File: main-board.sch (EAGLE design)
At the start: 54 parts, among them IC1 MEGA328-PB, IC2 MCP73831, IC3 LE33, Q1 3,6864 MHz, Q4 TSM2302CX, T1 IRF7306

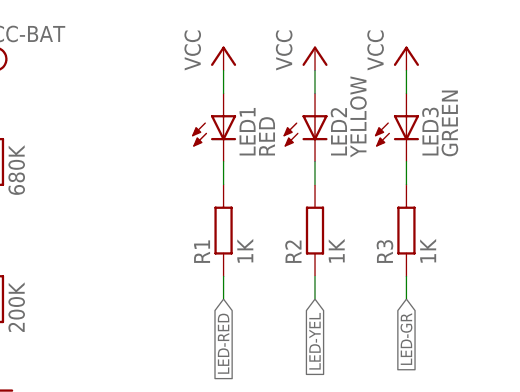
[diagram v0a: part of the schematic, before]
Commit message: Create nice place views.
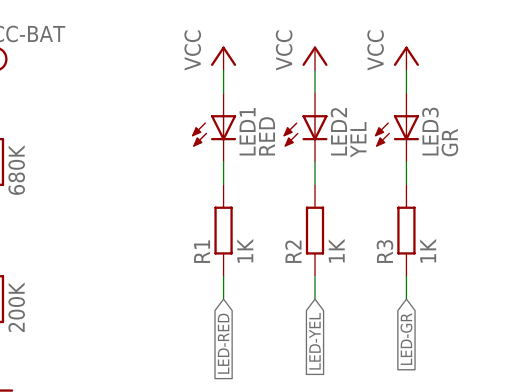
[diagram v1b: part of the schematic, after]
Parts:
- LED2: value YELLOW -> YEL
- LED3: value GREEN -> GR
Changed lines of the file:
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@@
 <part name="GND2" library="supply1" deviceset="GND" device=""/>
 <part name="LED1" library="led" deviceset="LED" device="CHIP-LED0805" value="RED"/>
-<part name="LED2" library="led" deviceset="LED" device="CHIP-LED0805" value="YELLOW"/>
-<part name="LED3" library="led" deviceset="LED" device="CHIP-LED0805" value="GREEN"/>
+<part name="LED2" library="led" deviceset="LED" device="CHIP-LED0805" value="YEL"/>
+<part name="LED3" library="led" deviceset="LED" device="CHIP-LED0805" value="GR"/>
 <part name="P+2" library="supply1" deviceset="VCC" device=""/>
 <part name="P+3" library="supply1" deviceset="VCC" device=""/>

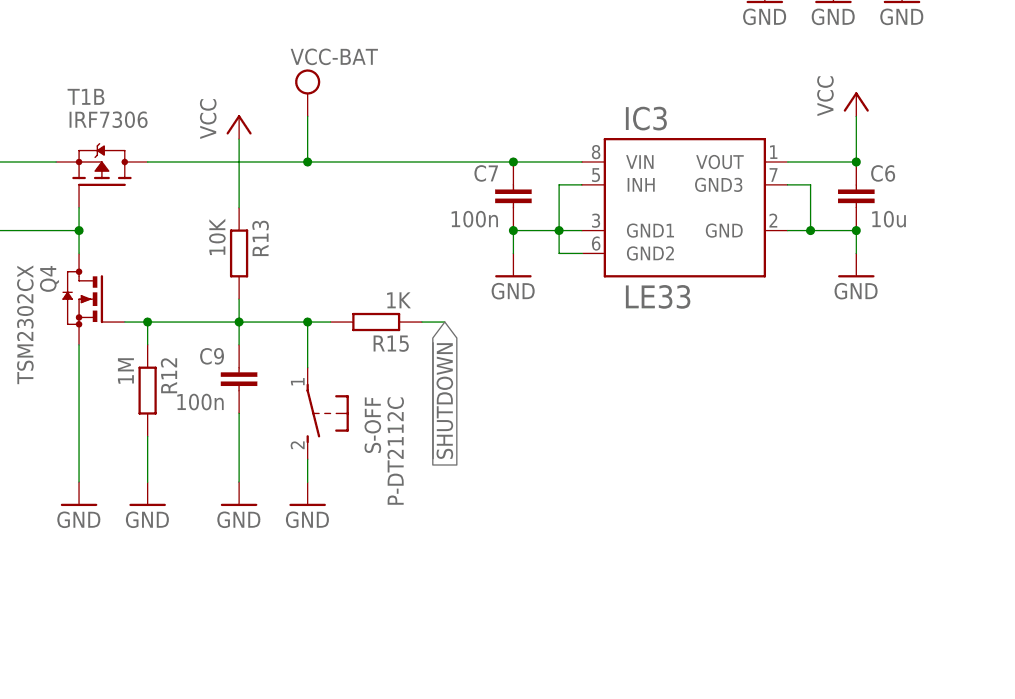
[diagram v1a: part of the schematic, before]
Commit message: Fix shutdown circuit.
Shutting down from CPU should work now.
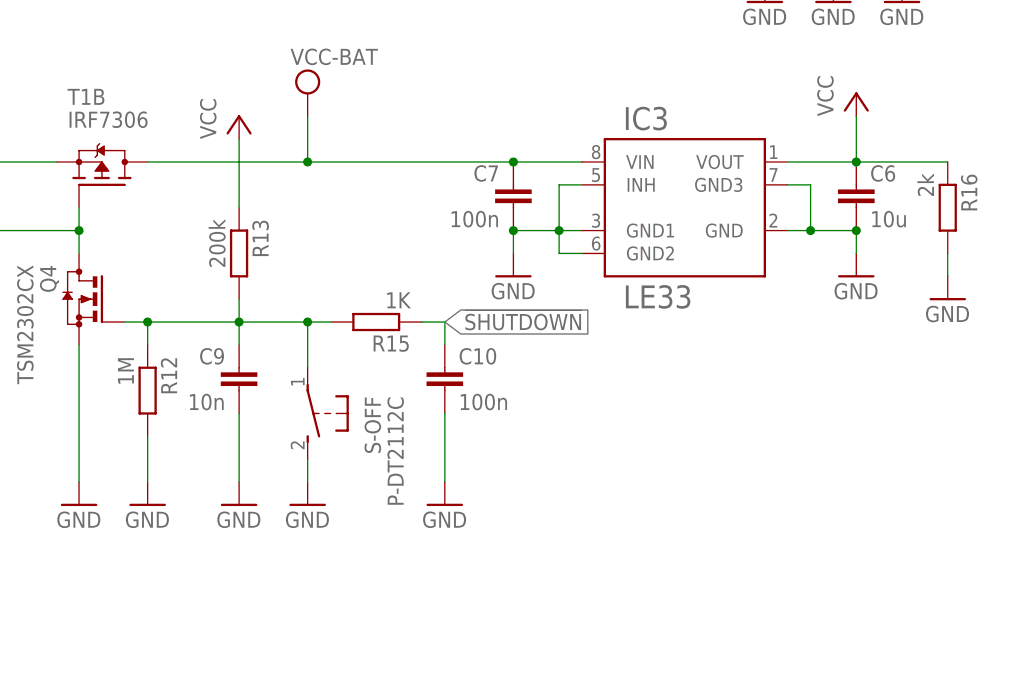
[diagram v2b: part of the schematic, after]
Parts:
- added C10: 100n, rcl:C-EUC0805
- added R16: 2k, rcl:R-EU_R0805
- C9: value 100n -> 10n
- R13: value 10K -> 200k
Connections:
- net !SHUTDOWN: now also C10.1
- net GND: now also C10.2, R16.2
- net VCC: now also R16.1
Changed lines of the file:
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@@
 <attributes>
 <attribute name="AUTHOR" value="Jan Horacek"/>
-<attribute name="VERSION" value="1.2"/>
+<attribute name="VERSION" value="1.3"/>
 </attributes>
 <variantdefs>
@@
 <part name="C8" library="rcl" deviceset="C-EU" device="C0805" value="10u"/>
 <part name="R12" library="rcl" deviceset="R-EU_" device="R0805" value="1M"/>
-<part name="R13" library="rcl" deviceset="R-EU_" device="R0805" value="10K"/>
-<part name="C9" library="rcl" deviceset="C-EU" device="C0805" value="100n"/>
+<part name="R13" library="rcl" deviceset="R-EU_" device="R0805" value="200k"/>
+<part name="C9" library="rcl" deviceset="C-EU" device="C0805" value="10n"/>
 <part name="R10" library="rcl" deviceset="R-EU_" device="R0805" value="100K"/>
 <part name="Q4" library="transistor-small-signal" deviceset="BSS123" device="" value="TSM2302CX"/>
@@
 <variant name="BASIC" populate="no"/>
 </part>
+<part name="C10" library="rcl" deviceset="C-EU" device="C0805" value="100n"/>
+<part name="GND19" library="supply1" library_urn="urn:adsk.eagle:library:371" deviceset="GND" device=""/>
+<part name="R16" library="rcl" deviceset="R-EU_" device="R0805" value="2k"/>
+<part name="GND20" library="supply1" deviceset="GND" device=""/>
 </parts>
 <sheets>
@@
 <attribute name="VALUE" x="50.5714" y="48.26" size="1.778" layer="96" rot="R90"/>
 </instance>
+<instance part="C10" gate="G$1" x="193.04" y="48.26"/>
+<instance part="GND19" gate="1" x="193.04" y="33.02"/>
+<instance part="R16" gate="G$1" x="248.92" y="66.04" rot="R270"/>
+<instance part="GND20" gate="1" x="248.92" y="55.88"/>
 </instances>
 <busses>
@@
 <wire x1="111.76" y1="58.42" x2="111.76" y2="66.04" width="0.1524" layer="91"/>
 </segment>
+<segment>
+<pinref part="GND19" gate="1" pin="GND"/>
+<pinref part="C10" gate="G$1" pin="2"/>
+<wire x1="193.04" y1="35.56" x2="193.04" y2="43.18" width="0.1524" layer="91"/>
+</segment>
+<segment>
+<pinref part="GND20" gate="1" pin="GND"/>
+<pinref part="R16" gate="G$1" pin="2"/>
+<wire x1="248.92" y1="58.42" x2="248.92" y2="60.96" width="0.1524" layer="91"/>
+</segment>
 </net>
 <net name="VCC" class="2">
@@
 <pinref part="C6" gate="G$1" pin="1"/>
 <junction x="238.76" y="71.12"/>
+<pinref part="R16" gate="G$1" pin="1"/>
+<wire x1="238.76" y1="71.12" x2="248.92" y2="71.12" width="0.1524" layer="91"/>
 </segment>
 <segment>
@@
 <pinref part="R15" gate="G$1" pin="1"/>
 <wire x1="193.04" y1="53.34" x2="190.5" y2="53.34" width="0.1524" layer="91"/>
-<label x="193.04" y="53.34" size="1.778" layer="95" rot="R270" xref="yes"/>
-</segment>
-<segment>
+<label x="193.04" y="53.34" size="1.778" layer="95" xref="yes"/>
+<pinref part="C10" gate="G$1" pin="1"/>
+<wire x1="193.04" y1="50.8" x2="193.04" y2="53.34" width="0.1524" layer="91"/>
+</segment>
+<segment>

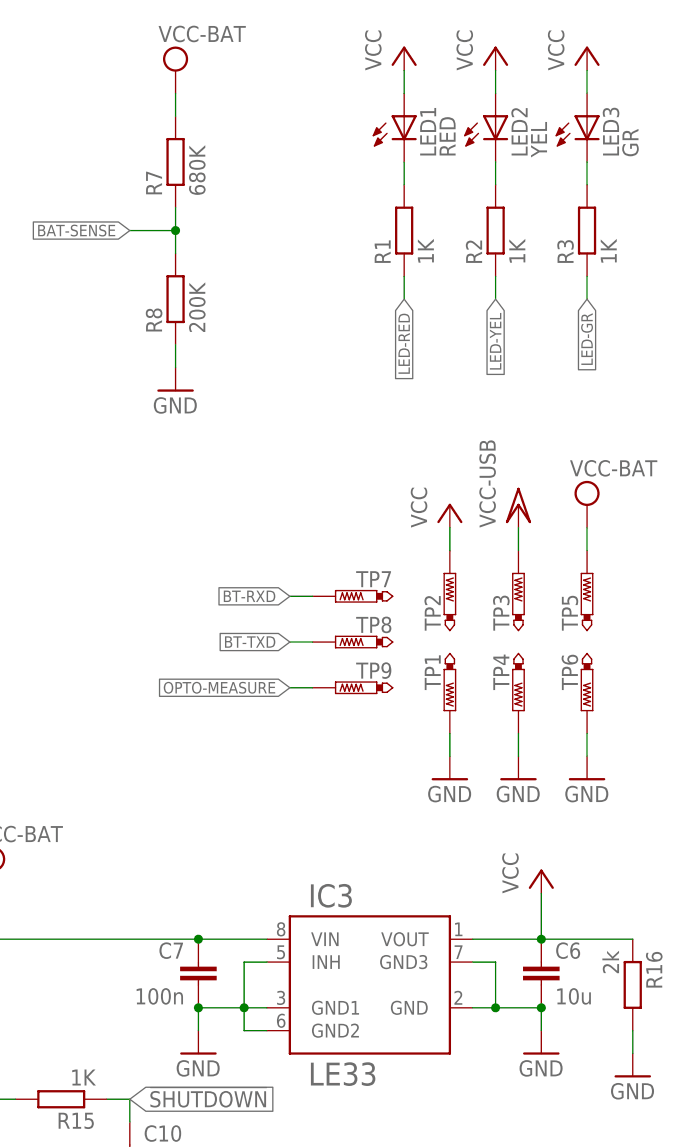
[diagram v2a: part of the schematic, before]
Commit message: Change voltage divisor (use LDO as reference).
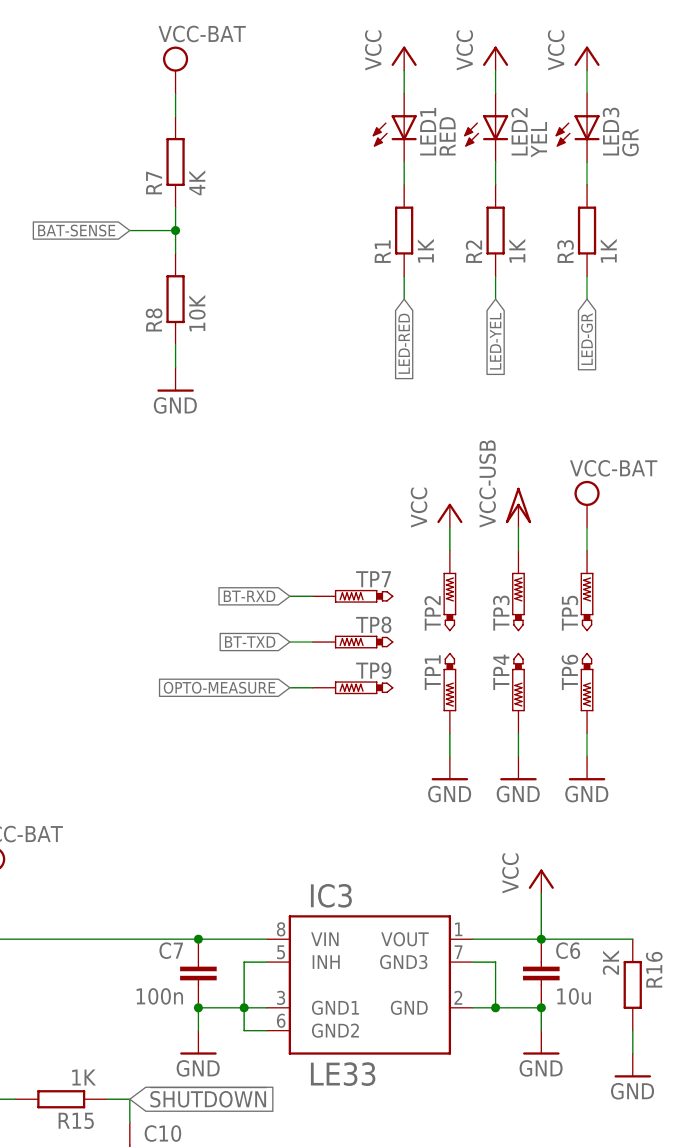
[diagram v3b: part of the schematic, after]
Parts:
- R16: value 2k -> 2K
- R7: value 680K -> 4K
- R8: value 200K -> 10K
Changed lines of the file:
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@@
 <part name="R6" library="rcl" deviceset="R-EU_" device="R0805" value="10K"/>
 <part name="P+8" library="supply1" deviceset="VCC" device=""/>
-<part name="R7" library="rcl" deviceset="R-EU_" device="R0805" value="680K"/>
-<part name="R8" library="rcl" deviceset="R-EU_" device="R0805" value="200K"/>
+<part name="R7" library="rcl" deviceset="R-EU_" device="R0805" value="4K"/>
+<part name="R8" library="rcl" deviceset="R-EU_" device="R0805" value="10K"/>
 <part name="SUPPLY1" library="supply2" deviceset="VCC" device="" value="VCC-BAT"/>
 <part name="GND7" library="supply1" deviceset="GND" device=""/>
@@
 <part name="C10" library="rcl" deviceset="C-EU" device="C0805" value="100n"/>
 <part name="GND19" library="supply1" library_urn="urn:adsk.eagle:library:371" deviceset="GND" device=""/>
-<part name="R16" library="rcl" deviceset="R-EU_" device="R0805" value="2k"/>
+<part name="R16" library="rcl" deviceset="R-EU_" device="R0805" value="2K"/>
 <part name="GND20" library="supply1" deviceset="GND" device=""/>
 </parts>

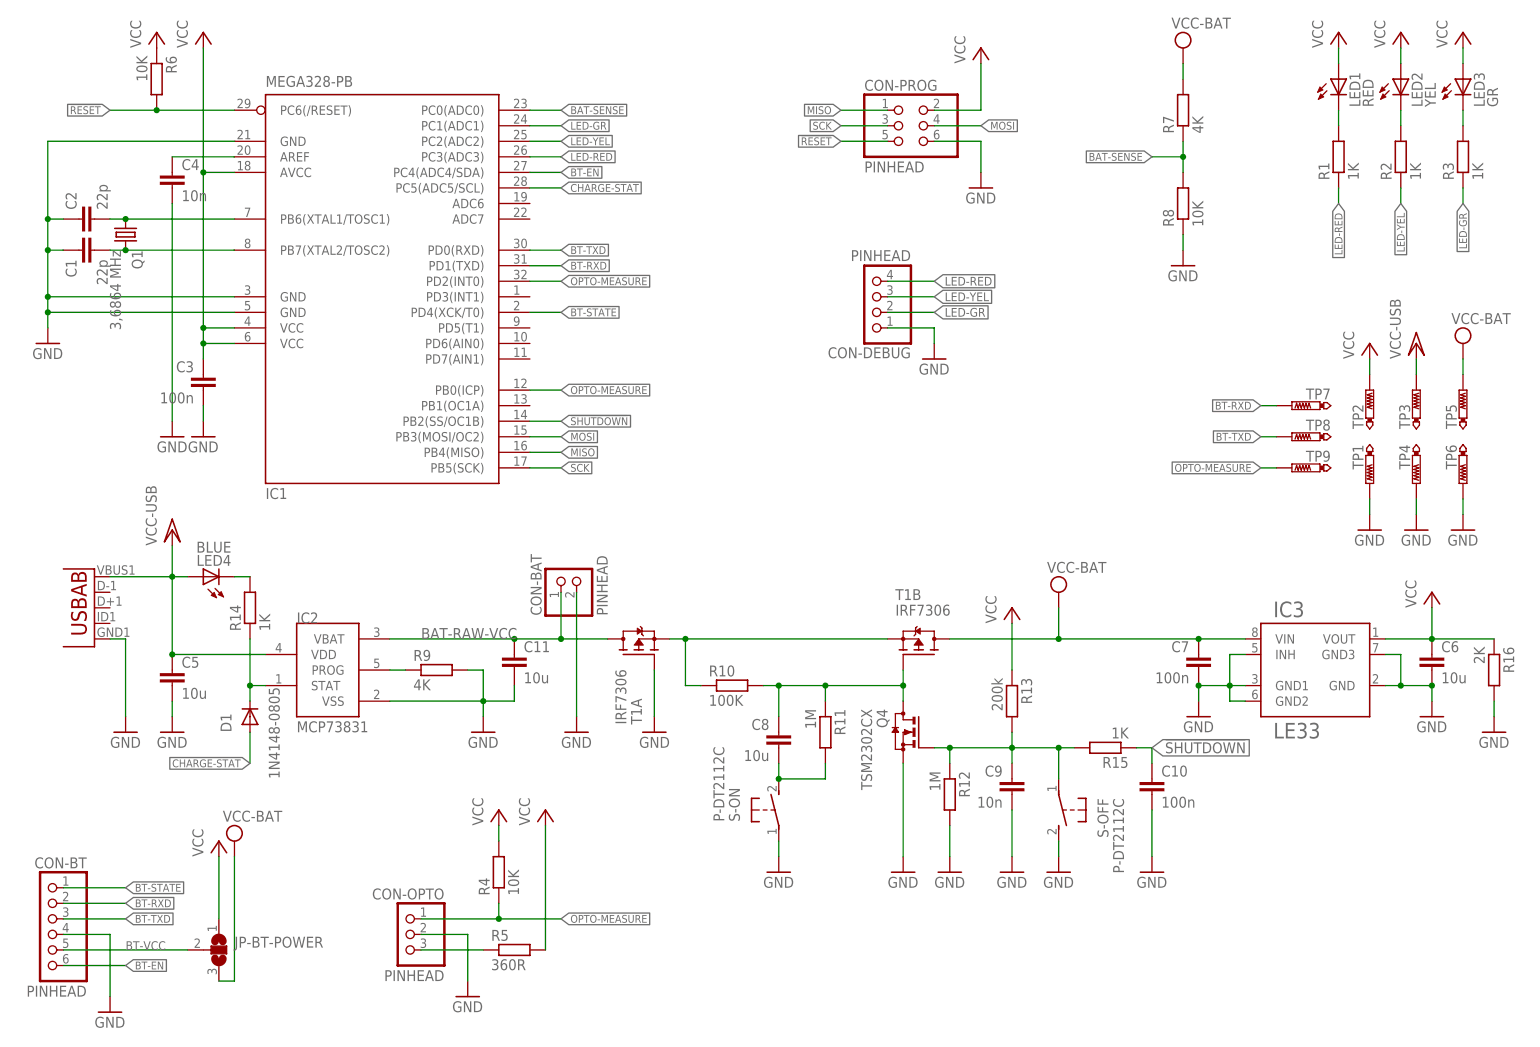
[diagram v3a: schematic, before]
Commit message: 4K -> 3K9.
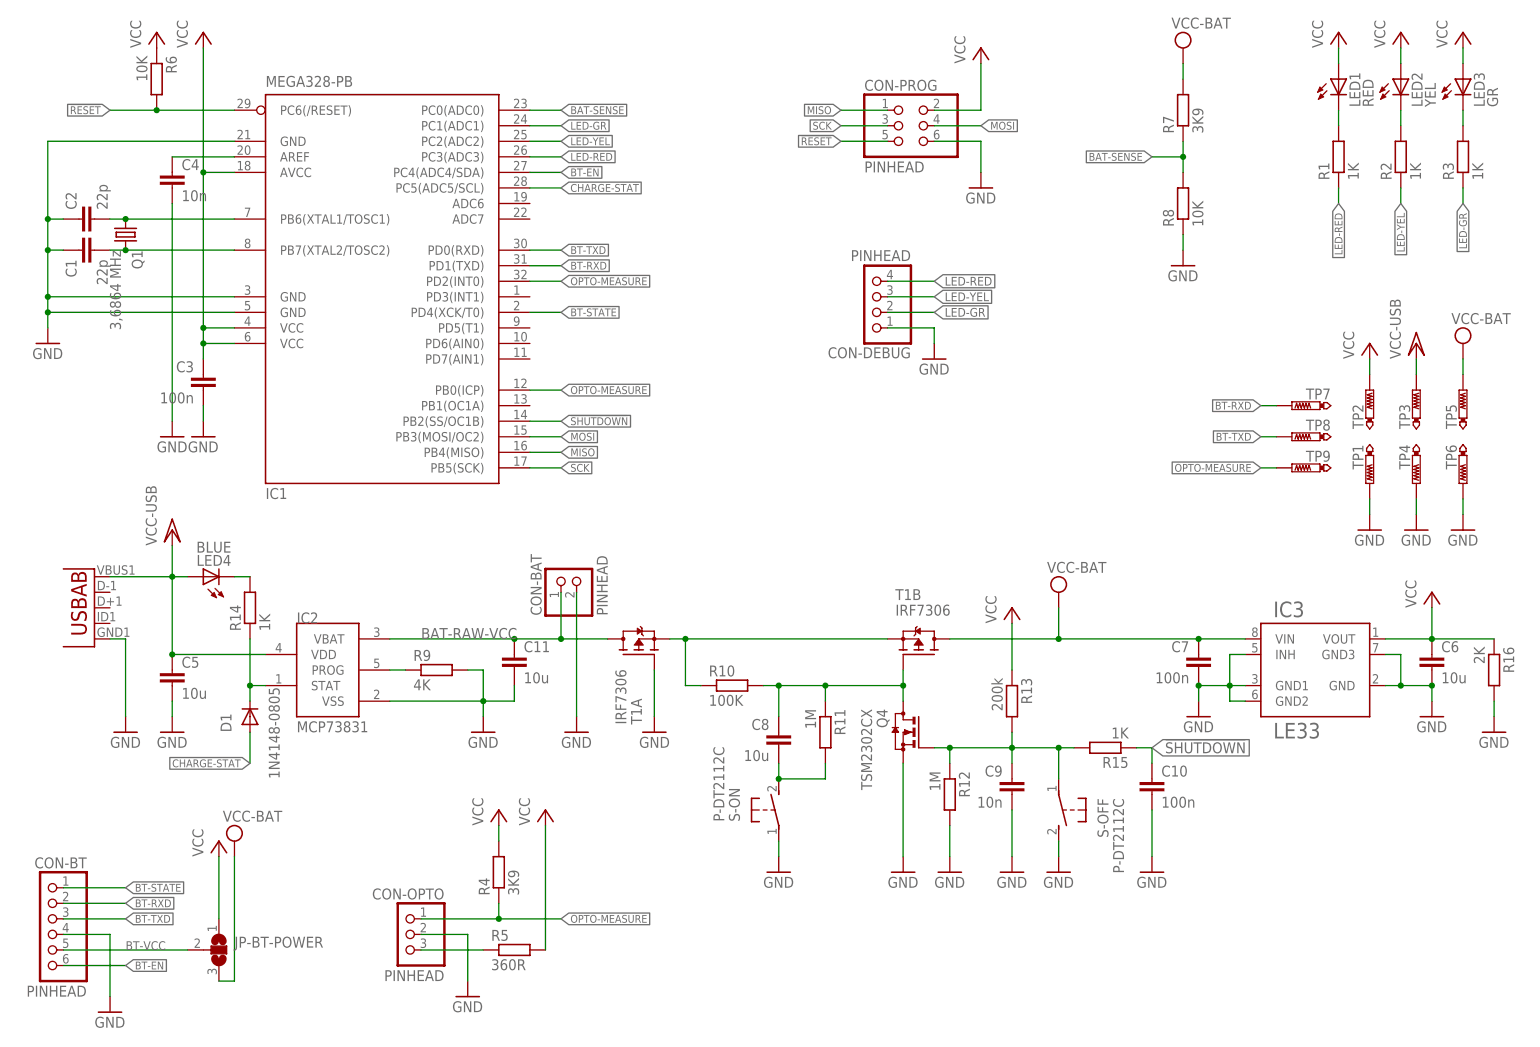
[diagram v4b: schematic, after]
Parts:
- R4: value 10K -> 3K9
- R7: value 4K -> 3K9
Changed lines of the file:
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@@
 <part name="CON-OPTO" library="pinhead" deviceset="PINHD-1X3" device="" value="PINHEAD"/>
 <part name="GND5" library="supply1" deviceset="GND" device=""/>
-<part name="R4" library="rcl" deviceset="R-EU_" device="R0805" value="10K"/>
+<part name="R4" library="rcl" deviceset="R-EU_" device="R0805" value="3K9"/>
 <part name="R5" library="rcl" deviceset="R-EU_" device="R0805" value="360R"/>
 <part name="P+6" library="supply1" deviceset="VCC" device=""/>
@@
 <part name="R6" library="rcl" deviceset="R-EU_" device="R0805" value="10K"/>
 <part name="P+8" library="supply1" deviceset="VCC" device=""/>
-<part name="R7" library="rcl" deviceset="R-EU_" device="R0805" value="4K"/>
+<part name="R7" library="rcl" deviceset="R-EU_" device="R0805" value="3K9"/>
 <part name="R8" library="rcl" deviceset="R-EU_" device="R0805" value="10K"/>
 <part name="SUPPLY1" library="supply2" deviceset="VCC" device="" value="VCC-BAT"/>

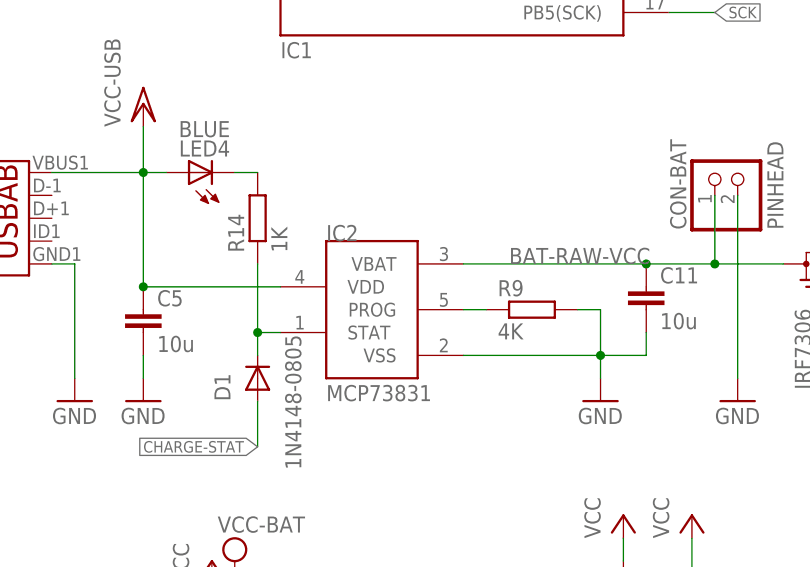
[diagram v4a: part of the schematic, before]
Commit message: Update values of resistors.
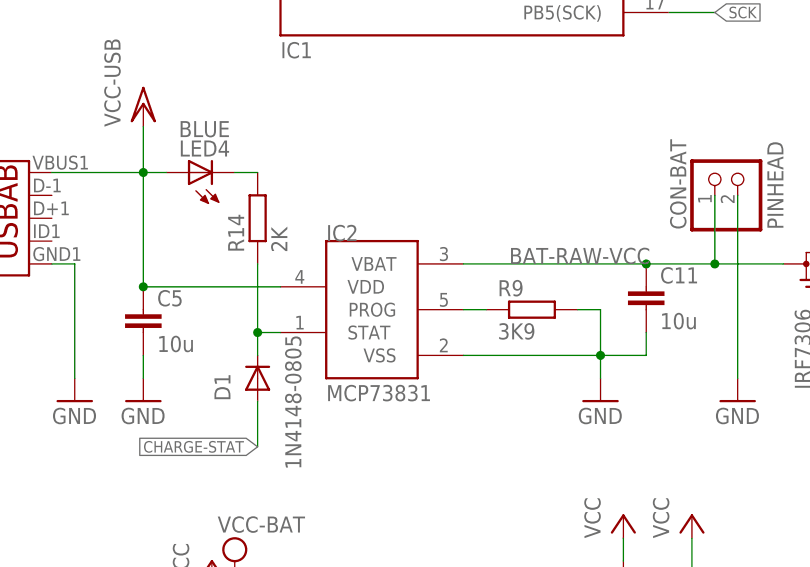
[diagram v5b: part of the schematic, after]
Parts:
- R14: value 1K -> 2K
- R9: value 4K -> 3K9
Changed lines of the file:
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@@
 <part name="IC2" library="mcp73831" deviceset="MCP73831" device=""/>
 <part name="GND9" library="supply1" deviceset="GND" device=""/>
-<part name="R9" library="rcl" deviceset="R-EU_" device="R0805" value="4K"/>
+<part name="R9" library="rcl" deviceset="R-EU_" device="R0805" value="3K9"/>
 <part name="P+9" library="supply1" deviceset="VCC/2" device="" value="VCC-USB"/>
 <part name="GND10" library="supply1" deviceset="GND" device=""/>
@@
 <part name="P+12" library="supply1" deviceset="VCC" device=""/>
 <part name="LED4" library="led" deviceset="LED" device="CHIP-LED0805" value="BLUE"/>
-<part name="R14" library="rcl" deviceset="R-EU_" device="R0805" value="1K"/>
+<part name="R14" library="rcl" deviceset="R-EU_" device="R0805" value="2K"/>
 <part name="C8" library="rcl" deviceset="C-EU" device="C0805" value="10u"/>
 <part name="R12" library="rcl" deviceset="R-EU_" device="R0805" value="1M"/>
